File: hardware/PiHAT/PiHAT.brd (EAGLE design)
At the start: 65 x 56.5 mm, 41 parts, among them U1 ATMEGA328P, U2 TSL2561, U3 OPA344, U4 MPL115A, U6 ADMP401, U7 SHT31-DIS, Y1 16MHZ

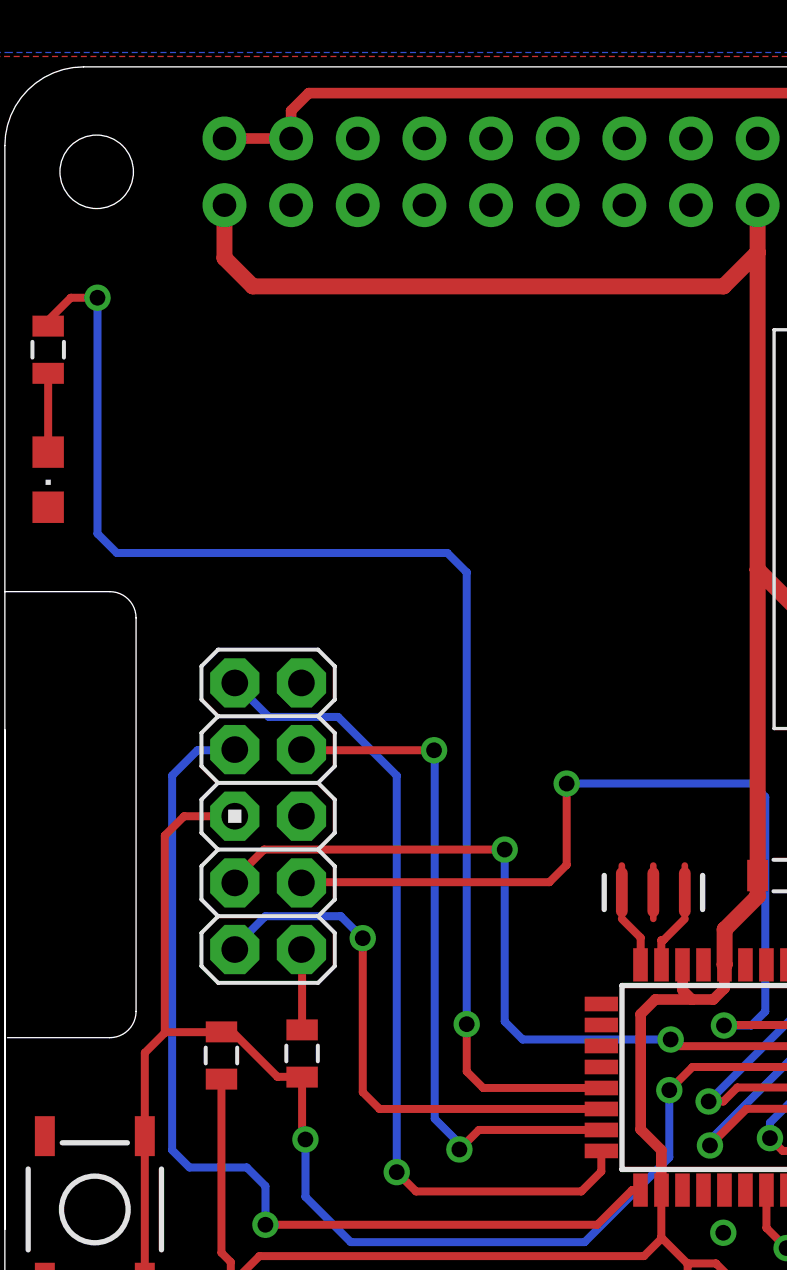
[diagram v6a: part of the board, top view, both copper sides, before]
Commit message: Updated silkscreen
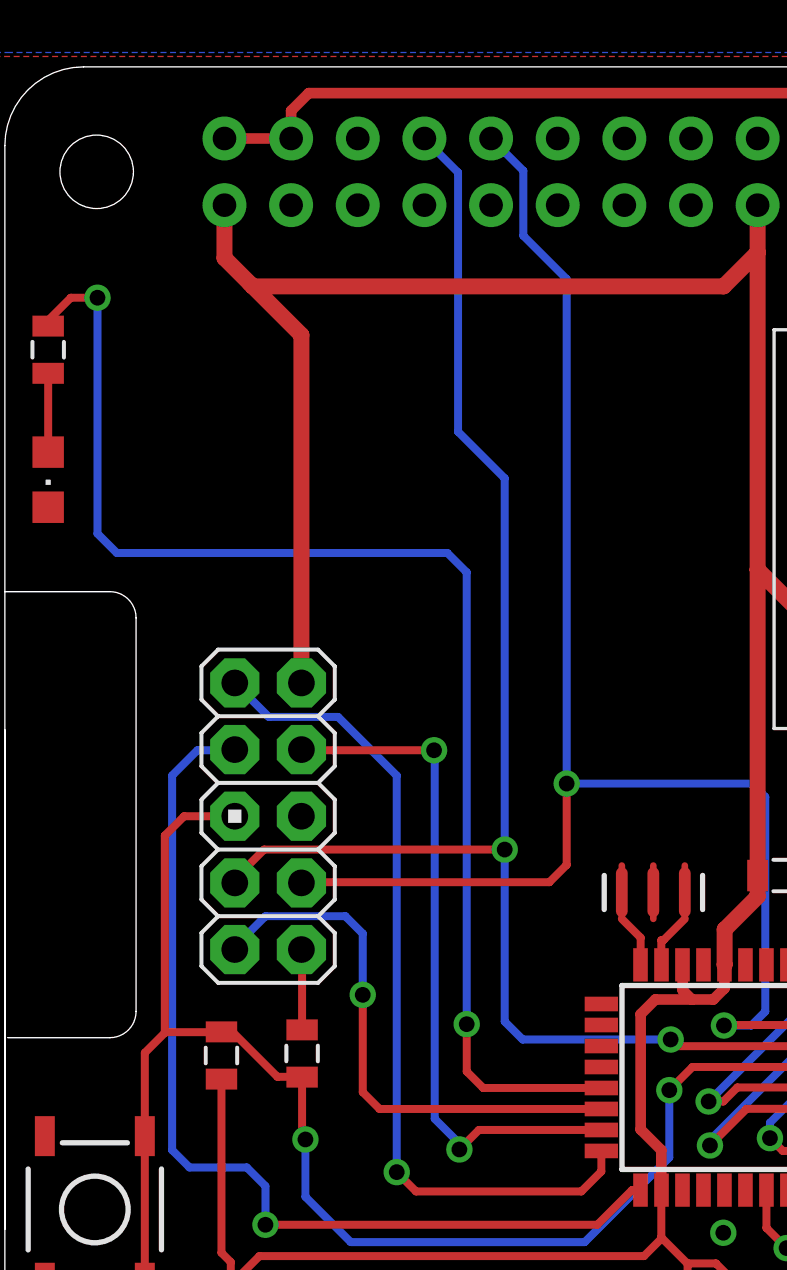
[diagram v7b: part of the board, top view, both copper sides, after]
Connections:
- removed net PWR: J2.2
- removed net RXD: RPI1.10
- removed net TXD: RPI1.8
- net RX: now also RPI1.8
- net TX: now also RPI1.10
- net VCC: now also J2.2
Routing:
- net RX: track 30.1 -> 58.5 mm
- net TX: track 35.2 -> 60.9 mm
- net VCC: track 198.2 -> 214.0 mm
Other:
- board text added: "3.3V"
- board text added: "5V"
- board text added: "DTR"
- board text added: "GND"
- board text added: "ISP"
- board text added: "MISO"
- board text added: "MOSI"
- board text added: "RESET"
- board text added: "RX"
- board text added: "SCK"
- board text added: "SS"
- board text added: "TX"
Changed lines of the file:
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@@
 <text x="4.9276" y="39.497" size="0.8128" layer="121" font="vector" rot="R90" align="bottom-center">Status
 LED</text>
+<text x="8.4328" y="53.8734" size="0.8128" layer="121" font="vector" align="bottom-center">5V</text>
+<text x="8.5852" y="47.879" size="0.8128" layer="121" font="vector" align="bottom-center">3.3V</text>
+<text x="16.0782" y="53.9242" size="0.8128" layer="121" font="vector" align="bottom-center">TX</text>
+<text x="18.5928" y="53.8988" size="0.8128" layer="121" font="vector" align="bottom-center">RX</text>
+<text x="6.7818" y="31.9024" size="0.6096" layer="121" font="vector" rot="R90" align="bottom-center">MISO</text>
+<text x="6.3246" y="29.6164" size="0.6096" layer="121" font="vector" rot="R180" align="bottom-center">SCK</text>
+<text x="6.9088" y="26.8478" size="0.6096" layer="121" font="vector" rot="R90" align="bottom-center">RESET</text>
+<text x="6.4516" y="23.7236" size="0.6096" layer="121" font="vector" align="bottom-center">RX</text>
+<text x="6.5024" y="21.1328" size="0.6096" layer="121" font="vector" align="bottom-center">SS</text>
+<text x="14.1224" y="31.4452" size="0.6096" layer="121" font="vector" rot="SR0" align="bottom-center">3.3V</text>
+<text x="14.1732" y="28.9052" size="0.6096" layer="121" font="vector" rot="SR0" align="bottom-center">MOSI</text>
+<text x="13.9446" y="26.3652" size="0.6096" layer="121" font="vector" rot="SR0" align="bottom-center">GND</text>
+<text x="13.6398" y="23.8506" size="0.6096" layer="121" font="vector" rot="SR0" align="bottom-center">TX</text>
+<text x="13.9192" y="21.2598" size="0.6096" layer="121" font="vector" rot="SR0" align="bottom-center">DTR</text>
+<text x="10.2362" y="33.8328" size="0.8128" layer="121" font="vector" align="bottom-center">ISP</text>
 </plain>
 <attributes>
@@
 <attribute name="MPN" value="" x="-38.7096" y="65.913" size="1.778" layer="27" display="off"/>
 <attribute name="OC_NEWARK" value="unknown" x="-38.7096" y="65.913" size="1.778" layer="27" display="off"/>
-<attribute name="VALUE" x="35.0774" y="12.954" size="0.8128" layer="121" font="vector"/>
+<attribute name="VALUE" x="35.1282" y="15.2908" size="0.8128" layer="121" font="vector"/>
 </element>
 <element name="R6" library="SparkFun-Resistors" package="0805" value="10K" x="36.0934" y="16.9926" smashed="yes">
@@
 <attribute name="MPN" value="" x="-44.8056" y="68.5546" size="1.778" layer="27" display="off"/>
 <attribute name="OC_NEWARK" value="unknown" x="-44.8056" y="68.5546" size="1.778" layer="27" display="off"/>
-<attribute name="VALUE" x="35.1028" y="18.2626" size="0.8128" layer="121" font="vector"/>
+<attribute name="VALUE" x="35.2044" y="18.1102" size="0.8128" layer="121" font="vector"/>
 </element>
 <element name="C3" library="SparkFun-Passives" package="0805" value="0.1uF" x="25.1206" y="6.2992" smashed="yes" rot="R180">
@@
 </element>
 <element name="U4" library="SparkFun-Sensors" package="LGA8" value="MPL115A" x="35.814" y="4.1402" smashed="yes" rot="R180">
-<attribute name="VALUE" x="37.338" y="7.1882" size="0.8128" layer="121" font="vector" rot="R180"/>
+<attribute name="VALUE" x="32.639" y="6.858" size="0.8128" layer="121" font="vector" rot="R270"/>
 </element>
 <element name="C13" library="SparkFun-Passives" package="0805" value="0.1uF" x="39.4716" y="3.175" smashed="yes" rot="R270">
-<attribute name="VALUE" x="38.0746" y="4.191" size="0.8128" layer="121" font="vector" rot="R270"/>
+<attribute name="VALUE" x="40.5892" y="4.8514" size="0.8128" layer="121" font="vector" rot="R270"/>
 </element>
 <element name="C14" library="SparkFun-Passives" package="0805" value="0.1uF" x="37.8968" y="8.4328" smashed="yes">
-<attribute name="VALUE" x="36.8808" y="7.0358" size="0.8128" layer="121" font="vector"/>
+<attribute name="VALUE" x="36.6268" y="9.7282" size="0.8128" layer="121" font="vector"/>
 </element>
 <element name="MICS4514" library="MICS-4514_CO_and_NOx_Sensor_Breakout" package="SPARKFUN-SENSORS_MICS_10-SMD" value="SPARKFUN-SENSORS_MICS-4514" x="56.642" y="37.592" smashed="yes" rot="R270">
@@
 <via x="27.3812" y="10.795" extent="1-16" drill="0.6"/>
 <via x="39.243" y="6.3246" extent="1-16" drill="0.6"/>
-</signal>
-<signal name="TXD">
-<contactref element="RPI1" pad="8"/>
-</signal>
-<signal name="RXD">
-<contactref element="RPI1" pad="10"/>
+<wire x1="26.6256" y1="21.0058" x2="28.2256" y2="21.0058" width="0" layer="19" extent="1-1"/>
 </signal>
 <signal name="GPIO18">
@@
 <wire x1="36.9932" y1="5.9944" x2="37.014" y2="6.0152" width="0.3048" layer="1"/>
 <wire x1="8.37" y1="49.96" x2="8.37" y2="47.9418" width="0.6096" layer="1"/>
-<wire x1="8.37" y1="47.9418" x2="9.4488" y2="46.863" width="0.6096" layer="1"/>
+<wire x1="8.37" y1="47.9418" x2="9.3345" y2="46.9773" width="0.6096" layer="1"/>
+<wire x1="9.3345" y1="46.9773" x2="9.4488" y2="46.863" width="0.6096" layer="1"/>
 <wire x1="39.3082" y1="26.543" x2="39.3082" y2="30.0008" width="0.6096" layer="1"/>
 <wire x1="39.3082" y1="30.0008" x2="39.297" y2="30.012" width="0.6096" layer="1"/>
@@
 <wire x1="28.691" y1="24.4094" x2="28.691" y2="36.067" width="0.6096" layer="1"/>
 <wire x1="28.691" y1="36.067" x2="28.69" y2="36.068" width="0.6096" layer="1"/>
+<contactref element="J2" pad="2"/>
+<wire x1="11.303" y1="31.75" x2="11.303" y2="45.0088" width="0.6096" layer="1"/>
+<wire x1="11.303" y1="45.0088" x2="9.4488" y2="46.863" width="0.6096" layer="1"/>
 </signal>
 <signal name="D5">
@@
 <wire x1="25.019" y1="21.9456" x2="25.1014" y2="21.9456" width="0.3048" layer="1"/>
 <wire x1="25.1014" y1="21.9456" x2="25.9142" y2="22.7584" width="0.3048" layer="1"/>
-</signal>
-<signal name="PWR">
-<contactref element="J2" pad="2"/>
 </signal>
 <signal name="MISO">
@@
 <wire x1="19.05" y1="18.8468" x2="19.7358" y2="18.161" width="0.3048" layer="16"/>
 <wire x1="19.7358" y1="18.161" x2="25.3746" y2="18.161" width="0.3048" layer="16"/>
+<contactref element="RPI1" pad="8"/>
+<wire x1="15.99" y1="52.5" x2="15.99" y2="52.4884" width="0.3048" layer="16"/>
+<wire x1="15.99" y1="52.4884" x2="17.272" y2="51.2064" width="0.3048" layer="16"/>
+<wire x1="19.05" y1="25.4" x2="19.05" y2="39.5478" width="0.3048" layer="16"/>
+<wire x1="19.05" y1="39.5478" x2="17.272" y2="41.3258" width="0.3048" layer="16"/>
+<wire x1="17.272" y1="41.3258" x2="17.272" y2="51.2064" width="0.3048" layer="16"/>
 </signal>
 <signal name="TX">
@@
 <wire x1="21.4122" y1="27.9146" x2="28.4734" y2="27.9146" width="0.3048" layer="16"/>
 <wire x1="28.4734" y1="27.9146" x2="28.9814" y2="27.4066" width="0.3048" layer="16"/>
+<contactref element="RPI1" pad="10"/>
+<wire x1="21.4122" y1="27.9146" x2="21.4122" y2="47.1424" width="0.3048" layer="16"/>
+<wire x1="21.4122" y1="47.1424" x2="19.7612" y2="48.7934" width="0.3048" layer="16"/>
+<wire x1="19.7612" y1="48.7934" x2="19.7612" y2="51.2688" width="0.3048" layer="16"/>
+<wire x1="19.7612" y1="51.2688" x2="18.53" y2="52.5" width="0.3048" layer="16"/>
 </signal>
 <signal name="N$8">
@@
 <wire x1="8.763" y1="21.59" x2="8.763" y2="21.6916" width="0.3048" layer="16"/>
 <wire x1="8.763" y1="21.6916" x2="9.9314" y2="22.86" width="0.3048" layer="16"/>
-<wire x1="9.9314" y1="22.86" x2="12.8016" y2="22.86" width="0.3048" layer="16"/>
-<wire x1="12.8016" y1="22.86" x2="13.6398" y2="22.0218" width="0.3048" layer="16"/>
-<via x="13.6398" y="22.0218" extent="1-16" drill="0.6"/>
+<wire x1="9.9314" y1="22.86" x2="12.9794" y2="22.86" width="0.3048" layer="16"/>
 <wire x1="22.7268" y1="15.5194" x2="22.733" y2="15.5132" width="0.3048" layer="1"/>
 <wire x1="22.733" y1="15.5132" x2="14.281" y2="15.5132" width="0.3048" layer="1"/>
-<wire x1="14.281" y1="15.5132" x2="13.6398" y2="16.1544" width="0.3048" layer="1"/>
-<wire x1="13.6398" y1="16.1544" x2="13.6398" y2="22.0218" width="0.3048" layer="1"/>
+<wire x1="12.9794" y1="22.86" x2="13.6398" y2="22.1996" width="0.3048" layer="16"/>
+<wire x1="13.6398" y1="22.1996" x2="13.6398" y2="19.8628" width="0.3048" layer="16"/>
+<via x="13.6398" y="19.8628" extent="1-16" drill="0.6"/>
+<wire x1="13.6398" y1="19.8628" x2="13.6398" y2="16.1544" width="0.3048" layer="1"/>
+<wire x1="13.6398" y1="16.1544" x2="14.281" y2="15.5132" width="0.3048" layer="1"/>
 </signal>
 <signal name="N$2">
